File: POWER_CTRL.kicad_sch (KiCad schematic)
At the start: 34 parts, among them J901 2350514-8, J902 2350514-8, Q901 PMV20XNER, Q902 PMV20XNER, Q903 PMV20XNER, Q904 PMV20XNER, Q905 PMV20XNER, Q906 PMV20XNER, Q907 PMV20XNER, Q908 PMV20XNER

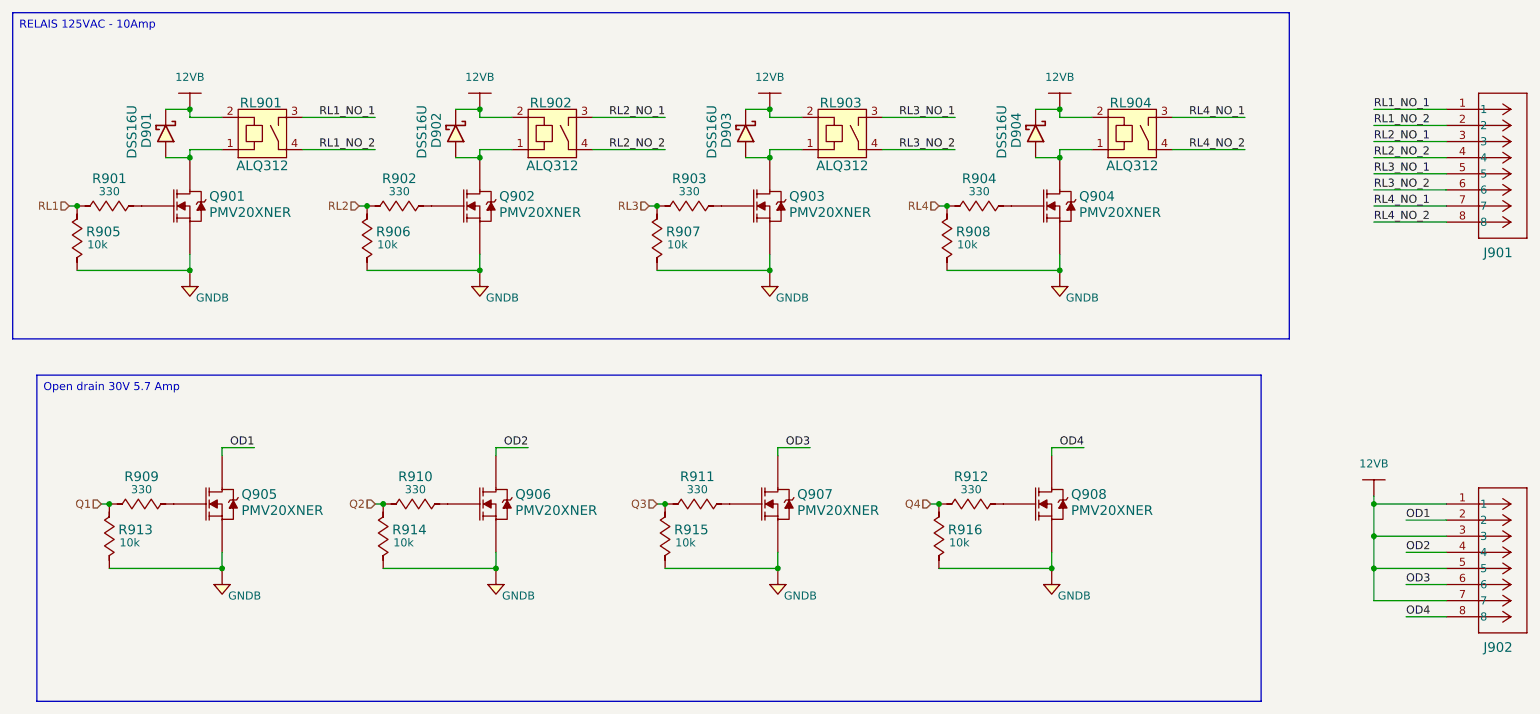
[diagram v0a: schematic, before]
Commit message: update schematic
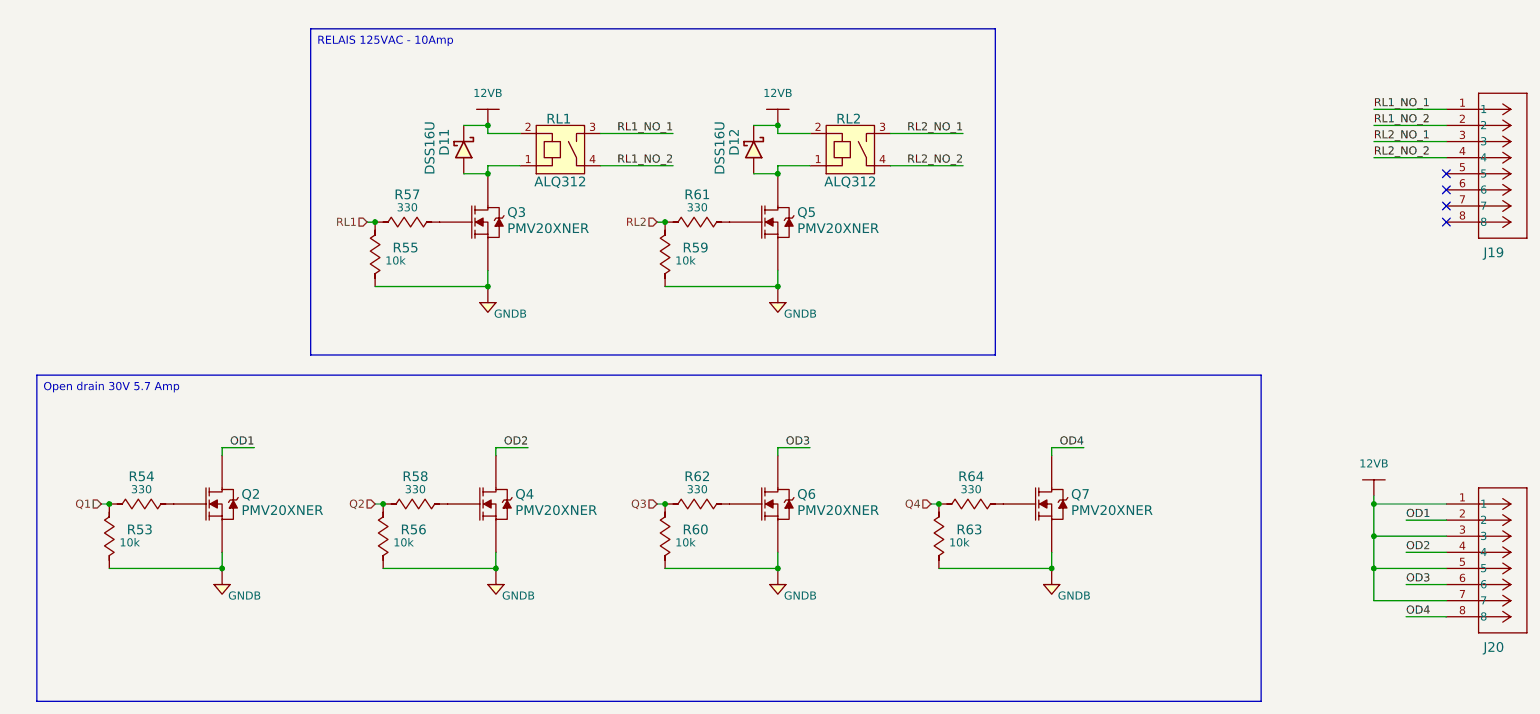
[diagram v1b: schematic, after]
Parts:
- removed D903, D904: DSS16U, Diodes:SOD-123FL, symbol Diodes:DSS16U
- removed Q903, Q904: PMV20XNER, IC:SOT-23-3, symbol Transistors:PMV20XNER
- removed R903, R904: RC0805JR-07330RL, Resistors:R0805, symbol Resistors:RC0805JR-07330RL
- removed R907, R908: RC0805JR-0710KL, Resistors:R0805, symbol Resistors:RC0805JR-0710KL
- removed RL903, RL904: ALQ312, Relays:ALQ312, symbol Relays:ALQ312
- renumbered D901 to D11, D902 to D12, J901 to J19, J902 to J20, Q905 to Q2, Q901 to Q3, Q906 to Q4, Q902 to Q5, Q907 to Q6, Q908 to Q7, R913 to R53, R909 to R54, R905 to R55, R914 to R56, R901 to R57, R910 to R58, R906 to R59, R915 to R60, R902 to R61, R911 to R62, R916 to R63, R912 to R64, RL901 to RL1, RL902 to RL2
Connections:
- net RL3_NO_1: no longer names the net of J19.5
- net RL3_NO_2: no longer names the net of J19.6
- net RL4_NO_1: no longer names the net of J19.7
- net RL4_NO_2: no longer names the net of J19.8
- no-connect marks 0 -> 4
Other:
- moved on the sheet: D11, D12, Q3, Q5, R55, R57, R59, R61, RL1, RL2

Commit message: finalisation de la schématique
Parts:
- renumbered D11 to D901, D12 to D902, J19 to J901, J20 to J902, Q3 to Q901, Q5 to Q902, Q2 to Q903, Q4 to Q904, Q6 to Q905, Q7 to Q906, R57 to R901, R61 to R902, R55 to R903, R59 to R904, R54 to R905, R58 to R906, R62 to R907, R64 to R908, R53 to R909, R56 to R910, R60 to R911, R63 to R912, RL1 to RL901, RL2 to RL902

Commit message: update
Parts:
- removed J901: 2350514-8, Connectors:CONN8_2350514-8_TEC, symbol Connectors:2350514-8
- added J801: 2350514-4, CONN4_1155650000_TEC, symbol Connectors:2350514-4
- renumbered D901 to D801, D902 to D802, J902 to J802, Q901 to Q801, Q902 to Q802, Q903 to Q803, Q904 to Q804, Q905 to Q805, Q906 to Q806, R901 to R801, R902 to R802, R903 to R803, R904 to R804, R905 to R805, R906 to R806, R907 to R807, R908 to R808, R909 to R809, R910 to R810, R911 to R811, R912 to R812, RL901 to RL801, RL902 to RL802
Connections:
- net RL1_NO_1: now also J801.1
- net RL1_NO_2: now also J801.2
- net RL2_NO_1: now also J801.3
- net RL2_NO_2: now also J801.4
- no-connect marks 4 -> 0
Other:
- moved on the sheet: J802
